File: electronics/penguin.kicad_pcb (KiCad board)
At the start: 4 copper layers, 88.2 x 61.1 mm, 137 parts, among them IC1 HY2120-AB, J1 USB_C_CONN, J10 MTR_HEADER_2, J2 CAM_HEADER, J3 BATT_BALANCE_HEADER, J4 TOF_HEADER, J6 IR_HEADER_1, J7 IR_HEADER_2, J8 BATT_CONN, J9 MTR_HEADER_1, Q1 AO3400A, Q2 SI2393DS, Q3 2N7002, Q4 FS8205A, SW1 SW_Boot, SW2 SW_Reset, U1 ESP32-S3-WROOM-1U-N8R8, U2 LP5907MFX-2.8, U3 LP5907MFX-1.2, U4 DRV8833PW, U5 MCP23017_ML, U6 TPS5405DR, U7 AMS1117-3.3, U8 DMP4065S-7

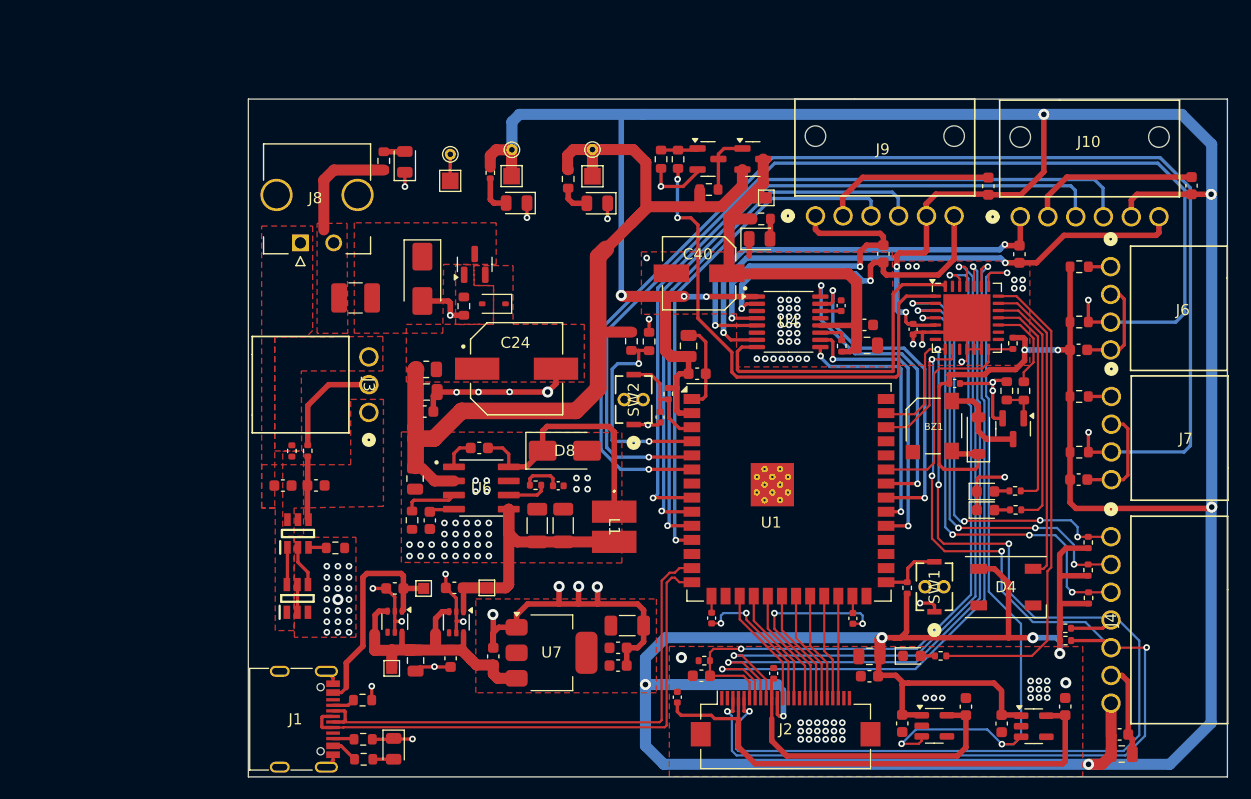
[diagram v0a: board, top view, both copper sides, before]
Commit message: finalize board outline
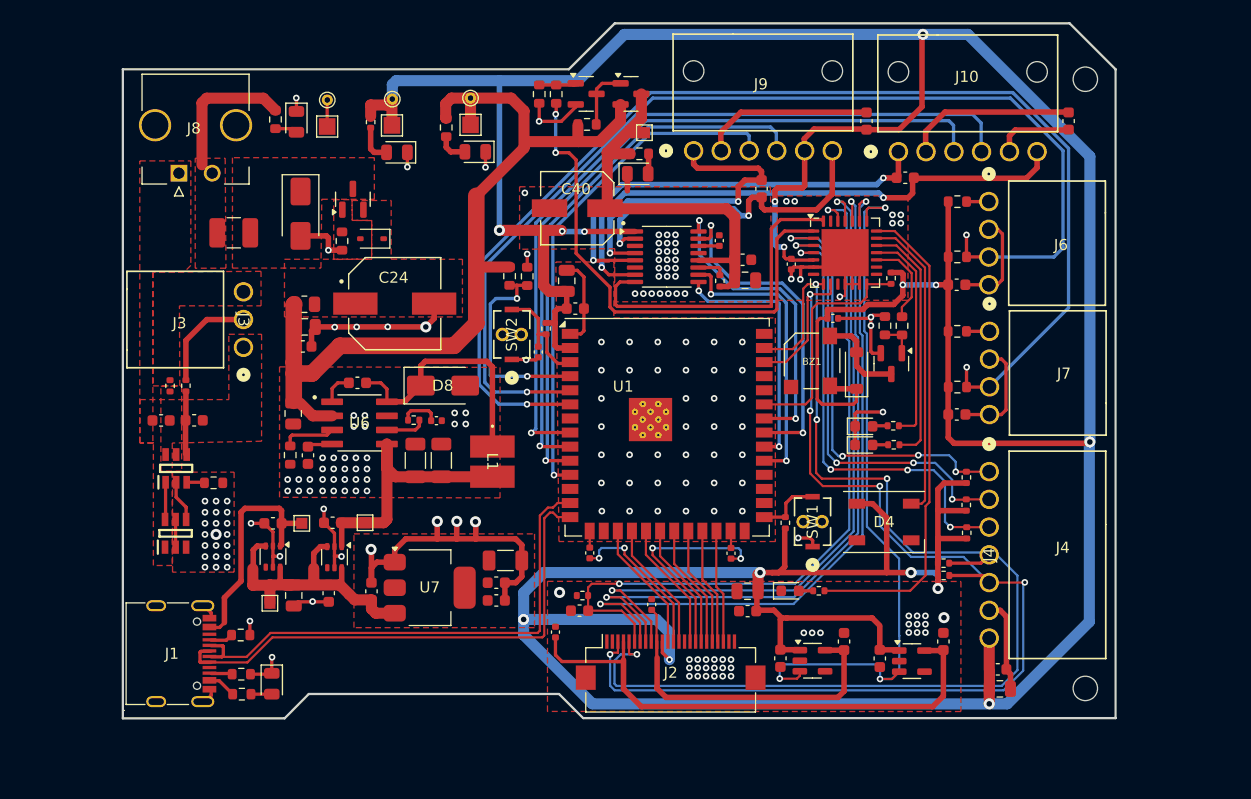
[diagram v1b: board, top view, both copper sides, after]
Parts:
- added H3: MountingHole, MountingHole:MountingHole_2.2mm_M2, F.Cu at (182.4, 63.5)
- added H4: MountingHole, MountingHole:MountingHole_2.2mm_M2, F.Cu at (182.4, 118.4)
- moved J3 12.7 mm to (106.5, 87.7)
- moved J8 12.6 mm to (100.7, 72.0)
- moved C9 12.6 mm to (143.3, 110.8)
- moved J1 12.6 mm to (99.8, 115.3)
- moved C19 12.5 mm to (180.9, 67.3)
- moved R2 12.5 mm to (133.8, 86.0)
- moved BZ1 12.4 mm to (157.8, 88.9)
- moved C21 12.4 mm to (149.5, 81.7)
- moved C39 12.4 mm to (129.3, 110.5)
- moved C4 12.4 mm to (136.4, 84.2)
- moved C47 12.4 mm to (170.8, 82.0)
- moved C6 12.4 mm to (160.7, 114.2)
- moved D10 12.4 mm to (142.1, 72.0)
- moved D2 12.4 mm to (162.4, 94.8)
- moved L1 12.4 mm to (129.0, 98.0)
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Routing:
- net +3V3: track 456.2 -> 444.9 mm, vias 16 -> 15
- net IR_DATA_2: track 114.9 -> 109.8 mm
- net VBATT: track 81.4 -> 78.1 mm
- net BATT_P: track 10.3 -> 12.8 mm
- net CAM_AVDD: track 47.0 -> 48.8 mm
- net CAM_DVDD: track 28.7 -> 30.1 mm
- net USB_P: track 48.6 -> 47.2 mm
- net IR_DATA_1: track 100.1 -> 98.7 mm
- net USB_N: track 48.5 -> 47.2 mm
- net CAM_EN: track 64.0 -> 65.2 mm
- net CAM_D4: track 9.20 -> 10.2 mm
- net Net-(J2-Pin_13): track 13.2 -> 14.2 mm
- net SDA: track 108.9 -> 107.8 mm
- net CAM_PWDN_EN: track 62.2 -> 63.3 mm
- net Net-(J2-Pin_17): track 18.7 -> 19.7 mm
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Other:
- board size 88.2 x 61.1 mm -> 89.5 x 62.6 mm
- board text added: "J3"
- board text added: "J4"

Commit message: silkscreen
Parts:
- added G***: LOGO, LOGO, F.Cu at (123.3, 76.0)
- added G***: LOGO, LOGO, F.Cu at (89.6, 69.0)
- added H1: MountingHole, MountingHole:MountingHole_2.2mm_M2, F.Cu at (118.3, 116.1)
- added H2: MountingHole, MountingHole:MountingHole_2.2mm_M2, F.Cu at (182.5, 63.7)
- C26: footprint Capacitor_SMD:C_0603_1608Metric -> Capacitor_SMD:C_0805_2012Metric
- C40: footprint EEH_ZK1V101XP:CAP_EEHZK1V101XP -> EEE_FK1V101P:CAP_EEEFK1V101P
- moved H3 65.8 mm to (118.2, 78.0)
- moved Q2 6.62 mm to (113.9, 80.4)
- moved D5 6.54 mm to (110.0, 81.9)
- moved R15 6.38 mm to (112.8, 83.9)
- moved D7 6.22 mm to (115.2, 83.4)
- moved FB1 4.58 mm to (116.0, 86.2), turned to -90 degrees
- moved C25 4.23 mm to (110.0, 89.5), turned to 180 degrees
- moved C24 3.06 mm to (123.1, 84.7)
- moved F1 2.39 mm to (105.2, 79.7)
- moved C26 1.93 mm to (110.0, 87.5), turned to 180 degrees
- moved D12 1.14 mm to (119.4, 69.5)
- moved R21 1.14 mm to (117.0, 66.8)
- moved TP6 1.14 mm to (119.0, 64.8)
- moved TP5 1.14 mm to (118.9, 67.1)
- moved D6 1.07 mm to (111.1, 66.3)
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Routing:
- net GND: track 190.4 -> 183.4 mm, vias 186 -> 355
- net VBATT: track 78.1 -> 83.3 mm
- net +3V3: track 444.9 -> 447.1 mm
- net IR_DATA_1: track 98.7 -> 96.7 mm, vias 2 -> 1
- net IR_DATA_2: track 109.8 -> 111.6 mm, vias 2 -> 1
- net MOTA_IN1: track 26.1 -> 27.6 mm
- net VBATT_SENSE: track 19.0 -> 20.2 mm
- net BATT_P: track 12.8 -> 11.7 mm
- net MOTB_IN1: track 30.3 -> 31.2 mm
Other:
- outline, holes or cut-outs redrawn
- board text added: "+"
- board text added: "-"
- board text added: "B"
- board text added: "BAL"
- board text added: "BATT"
- board text added: "CAM"
- board text added: "CAT"
- board text added: "EMI"
- board text added: "JS"
- board text added: "M2"
- board text added: "MOT A"
- board text added: "PGN-01"
- board text added: "PLUG"
- board text added: "SC"
- board text added: "SD"
- board text added: "USB"
- board text added: "VBAT"
- board text added: "VC"
- board text added: "VCC"
- board text added: "VM"
- board text added: "VS"
- board text added: "VSS"
- board text added: "WiFi"
- board text added: "autonomy"
- board text added: "boot"
- board text added: "bzz"
- board text added: "debug"
- board text added: "jeevan.26"
- board text added: "penguin"
- board text added: "reset"
- board text added: "sens"
- board text added: "stat"
- board text added: "v1"
- board text added: "vision"

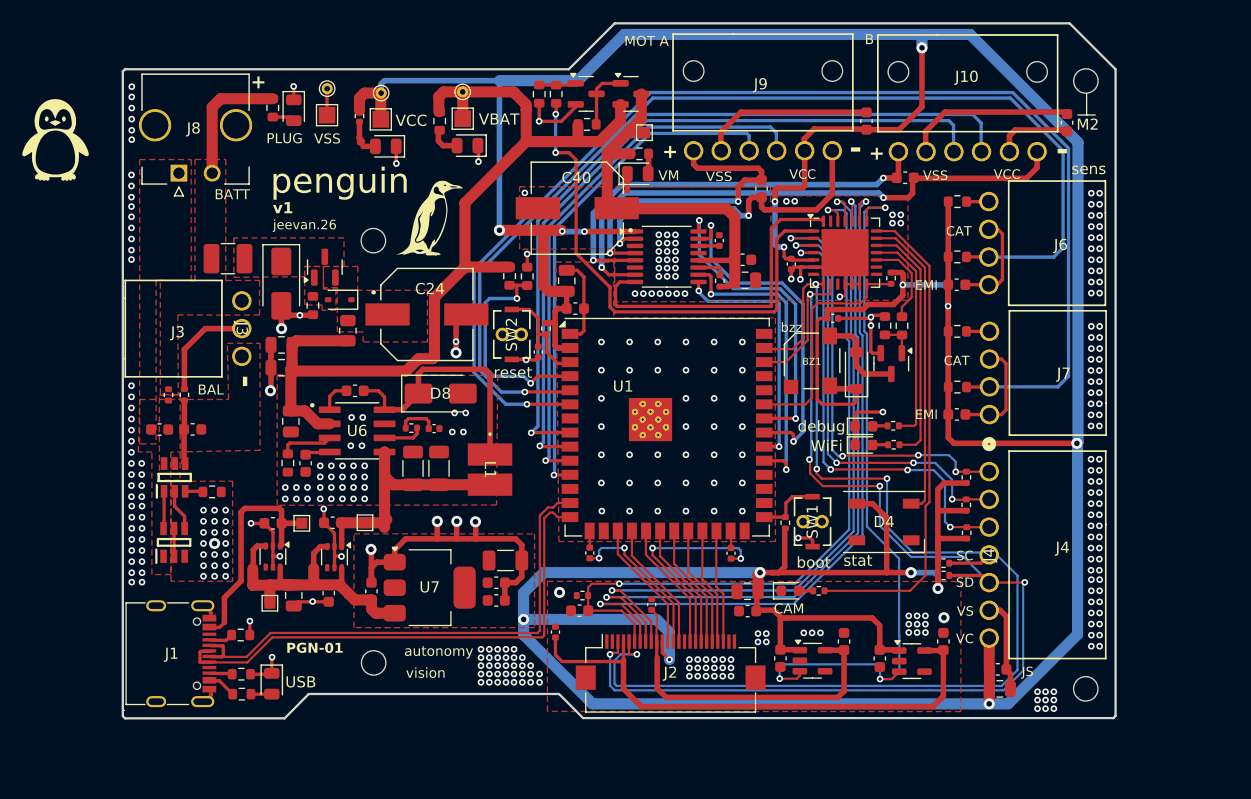
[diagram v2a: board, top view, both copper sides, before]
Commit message: finsih front silkscreen
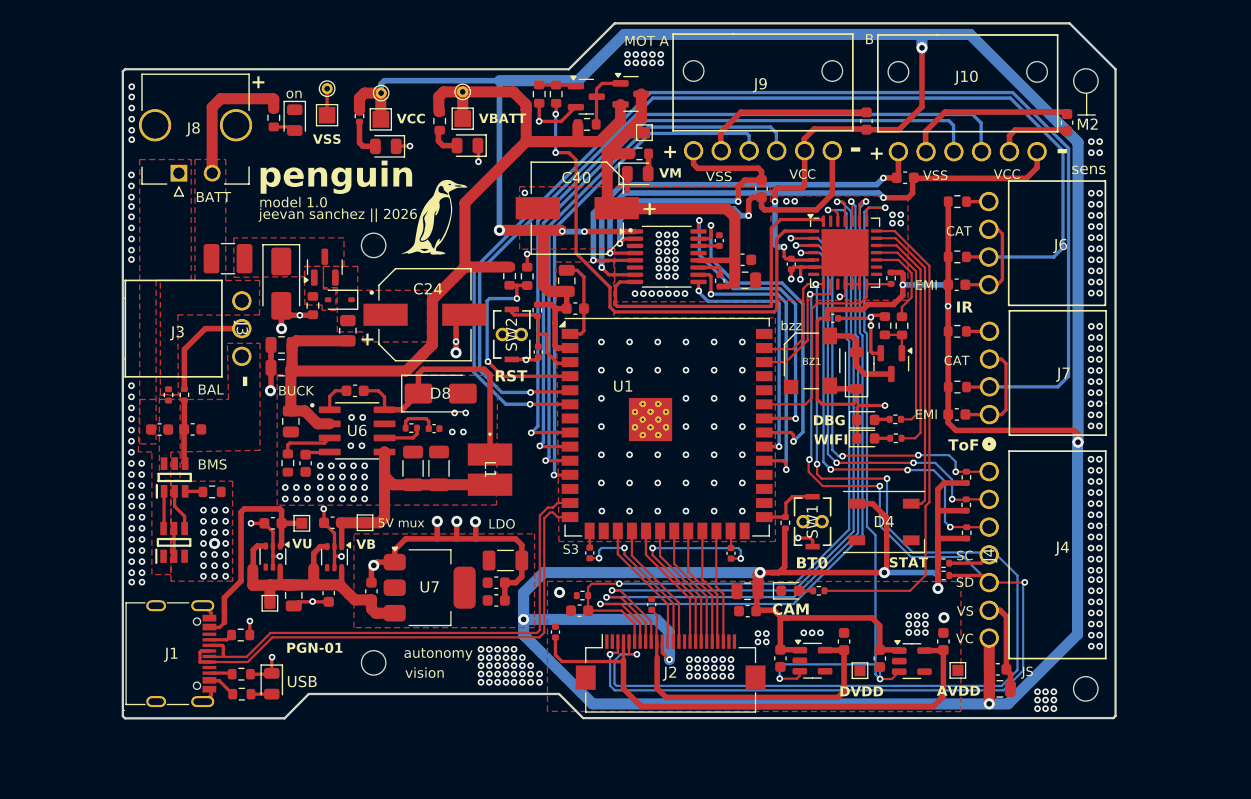
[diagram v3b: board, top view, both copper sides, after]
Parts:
- removed the G*** at (89.6, 69.0)
- added TP11: CAM_DVDD_TP_PAD, TestPoint:TestPoint_Pad_1.0x1.0mm, F.Cu at (162.1, 116.8)
- added TP12: CAM_AVDD_TP_PAD, TestPoint:TestPoint_Pad_1.0x1.0mm, F.Cu at (170.9, 116.8)
- moved R2 1.82 mm to (133.0, 84.3)
- moved D6 0.89 mm to (111.2, 67.2)
- moved R14 0.89 mm to (109.3, 67.0)
- moved D3 0.61 mm to (162.6, 95.9)
- moved D2 0.61 mm to (162.6, 94.2)
- moved R10 0.61 mm to (165.3, 95.9)
- moved R9 0.61 mm to (165.3, 94.2)
- moved G*** 0.43 mm to (123.7, 76.0)
- moved H3 0.43 mm to (118.3, 78.5)
- moved Q3 0.25 mm to (137.4, 65.1)
- moved C24 0.18 mm to (122.9, 84.7)
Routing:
- net GND: track 183.4 -> 179.0 mm, vias 355 -> 368
- net CAM_EN: track 65.2 -> 63.1 mm
- net +3V3: track 447.1 -> 448.3 mm
- net USB_N: track 47.2 -> 46.0 mm
- net VBATT_SENSE: track 20.2 -> 19.0 mm
- net 5V_BATT: track 24.7 -> 23.7 mm
- net BATT_P: track 11.7 -> 12.7 mm
- net DBG_LED: track 19.6 -> 18.7 mm
- net WIFI_LED: track 22.3 -> 21.5 mm
- net VBATT: track 83.3 -> 82.6 mm
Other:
- board text added: "5V mux"
- board text added: "AVDD"
- board text added: "BMS"
- board text added: "BT0"
- board text added: "BUCK"
- board text added: "DBG"
- board text added: "DVDD"
- board text added: "IR"
- board text added: "LDO"
- board text added: "RST"
- board text added: "S3"
- board text added: "STAT"
- board text added: "ToF"
- board text added: "VB"
- board text added: "VBATT"
- board text added: "VU"
- board text added: "WIFI"
- board text added: "jeevan sanchez || 2026"
- board text added: "model 1.0"
- board text added: "on"
- board text removed: "PLUG"
- board text removed: "VBAT"
- board text removed: "WiFi"
- board text removed: "boot"
- board text removed: "debug"
- board text removed: "jeevan.26"
- board text removed: "reset"
- board text removed: "stat"
- board text removed: "v1"

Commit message: finish back silkscreen
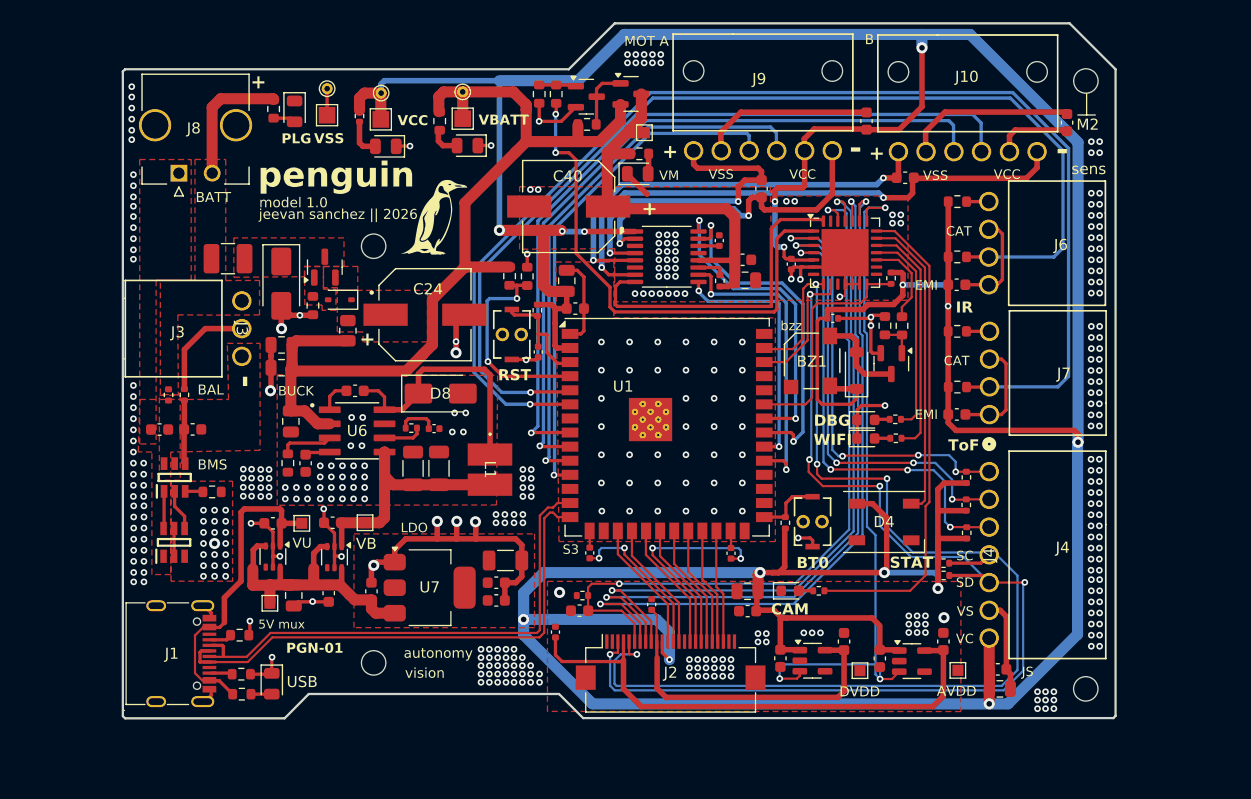
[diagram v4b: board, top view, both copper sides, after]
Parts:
- added ?: , clipboard:fc8df92e-a3b3-4f73-a46e-2aabbf2af471, B.Cu at (102.7, 66.8)
- added G***: LOGO, LOGO, B.Cu at (124.7, 109.1)
- moved C40 0.79 mm to (135.8, 75.0)
- moved D6 0.79 mm to (111.2, 66.4)
- moved R14 0.79 mm to (109.3, 66.2)
- moved R37 0.10 mm to (106.2, 113.6)
- moved H3 0.08 mm to (118.3, 78.5)
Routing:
- net 5V_USB: track 23.4 -> 30.0 mm
- net BATT_P: track 12.7 -> 11.8 mm
- net GND: track 179.0 -> 179.5 mm, vias 368 -> 401
- added copper zone on In1.Cu, net GND
- added copper zone on In2.Cu, net GND
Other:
- board text added: "ESP32-S3 core integrated WiFi & BLE"
- board text added: "IR-1"
- board text added: "IR-2"
- board text added: "MOT-A"
- board text added: "MOT-B"
- board text added: "PCB: 4L FR4, 1.6mm, HASL"
- board text added: "PLG"
- board text added: "TOF-1"
- board text added: "differential-drive robot controller"
- board text added: "engineered by Jeevan Sanchez in Toronto, CA"
- board text added: "github"
- board text added: "is 1.2V"
- board text added: "is 2.8V"
- board text added: "is 3.3V"
- board text added: "is 7.4V"
- board text added: "platform"
- board text added: "power 2S LiPo"
- board text added: "vision & multi-sensor processing"
- board text removed: "on"
